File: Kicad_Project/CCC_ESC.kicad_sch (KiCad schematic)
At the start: 228 parts, among them J1 Conn_01x07, J2 Conn_01x06, J3 Conn_01x06, J4 Conn_01x06, SW1 Conn_01x02, U1 NCP5183 / TF2190-TAH, U2 NCP5183 / TF2190-TAH, U3 NCP5183 / TF2190-TAH, U4 NCS20034DR2G, U5 STM32F401CCU6_Balckpill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

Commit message: more layout
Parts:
- removed TpGS1: TestPoint, TestPoint:TestPoint_THTPad_D4.0mm_Drill2.0mm, symbol Connector:TestPoint
- removed TpGS3, TpGS5: TestPoint, TestPoint:TestPoint_THTPad_D1.5mm_Drill0.7mm, symbol Connector:TestPoint
- D1, D2, D3: footprint Diode_SMD:D_SMA -> Diode_SMD:D_SOD-123; LCSC C412437 -> C5290222
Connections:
- net AU_GATESIG renamed DV1H_P
- net BU_GATESIG renamed DV2H_P
- net CU_GATESIG renamed DV3H_P
- net PHASE_A renamed DV1H_N
- net PHASE_B renamed DV2H_N
- net PHASE_C renamed DV3H_N

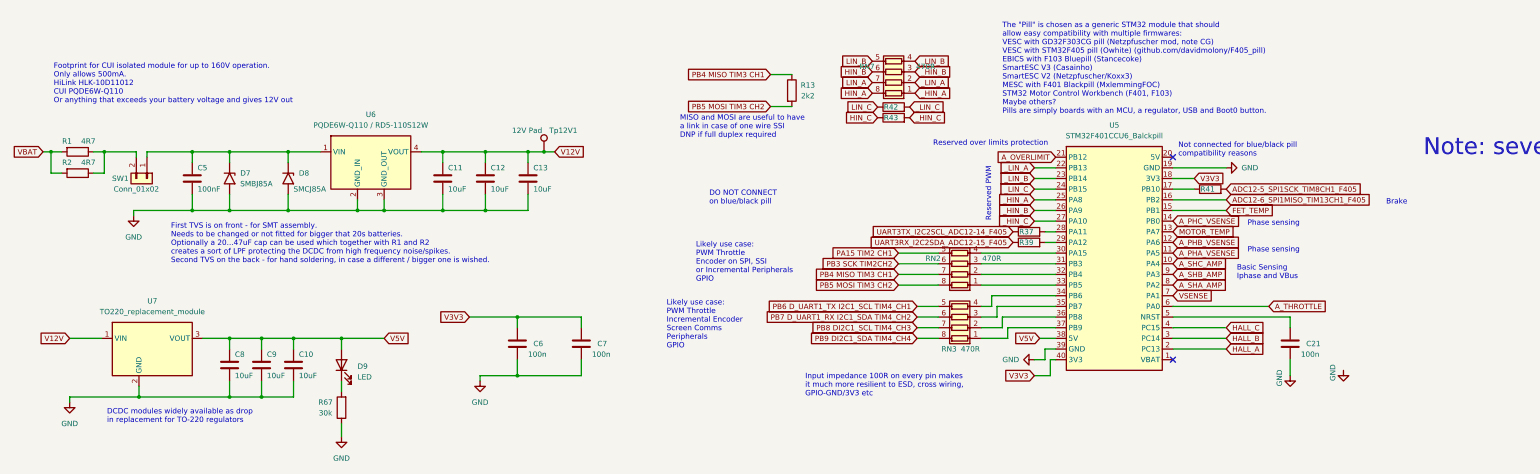
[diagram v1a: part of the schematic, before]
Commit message: added thermistor, 12v zener
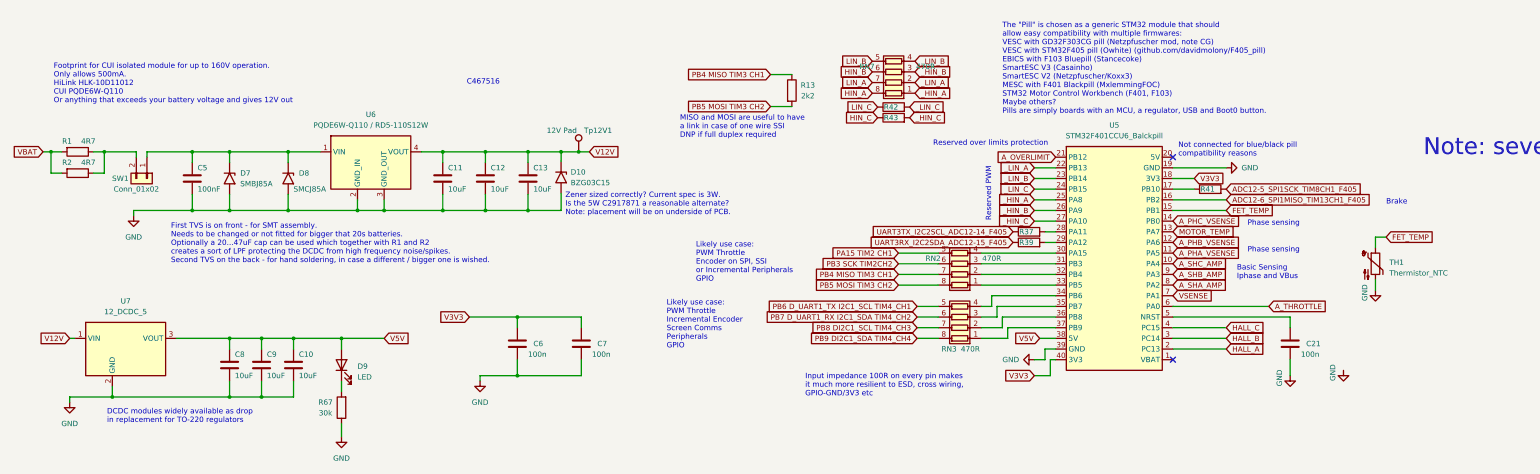
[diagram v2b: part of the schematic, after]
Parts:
- added D10: BZG03C15, Diode_SMD:D_SMA, symbol Diode:SM6T75A
- added TH1: Thermistor_NTC, Resistor_SMD:R_0603_1608Metric, symbol Device:Thermistor_NTC
- U7: value TO220_replacement_module -> 12_DCDC_5; footprint CCC_ESC_Custom_parts:TO220_replacement_module -> CCC_ESC_Custom_parts:12_DCDC_5
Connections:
- net FET_TEMP: now also TH1.1
- net GND: now also D10.2 (A2), TH1.2
- net V12V: now also D10.1 (A1)
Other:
- note added: "C467516"
- note added: "Zener sized correctly? Current spec is 3W. Is the 5W C2917871 a reasonable alternate? Note: placement will be on underside of PCB."
- note removed: "DO NOT CONNECT on blue/black pill"
- moved on the sheet: Tp12V1, U7

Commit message: added docs, prettied up fills
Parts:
- removed C31: 47pF, Capacitor_SMD:C_0603_1608Metric, symbol Device:C
- added C33: 10nF, Capacitor_SMD:C_0603_1608Metric, symbol Device:C
- C29, C30: value 47pF -> 10nF; LCSC C1671 -> C57112; MFR PT CL10C470JB8NNNC -> 0603B103K500NT
- CGS1, CGS10, CGS13, CGS16, CGS4, CGS7: value 6pF -> 6nF
- QB5: footprint Package_DFN_QFN:DFNW-8_L8.3-W8.4-P2.00-BL -> NVMTSC4D3N15MC:NVMTSC4D3N15MC
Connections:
- net A_PHA_VSENSE: now also C33.1; no longer C29.1
- net A_PHB_VSENSE: now also C29.1; no longer C30.1
- net A_PHC_VSENSE: now also C30.1
- net GND: now also C33.2
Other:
- note added: "Changes, not necessarily improvements: MOSFETS changed to DFNW format (NVMTSC4D3N15MC) Tidied up differential routing to shunt resistors and gate ressistors Added gate to source capacitors (CGS1-18) Protective 470 ohm resistors (RN7) between the drivers and PWM pill pins Phase sense caps (C29, C30, C33) set to 10nF for 10kHz range filtering Restructured vbat and gnd buses Restructured phase buses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"
- note added: "Use 10nF for a response in the 10kHz kind of range."
- note removed: "Note: several test points were removed in order to add additional components."
- moved on the sheet: C20, C22, C23, C24, C25, D4, D5, D6, R16, R17, R18, R19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

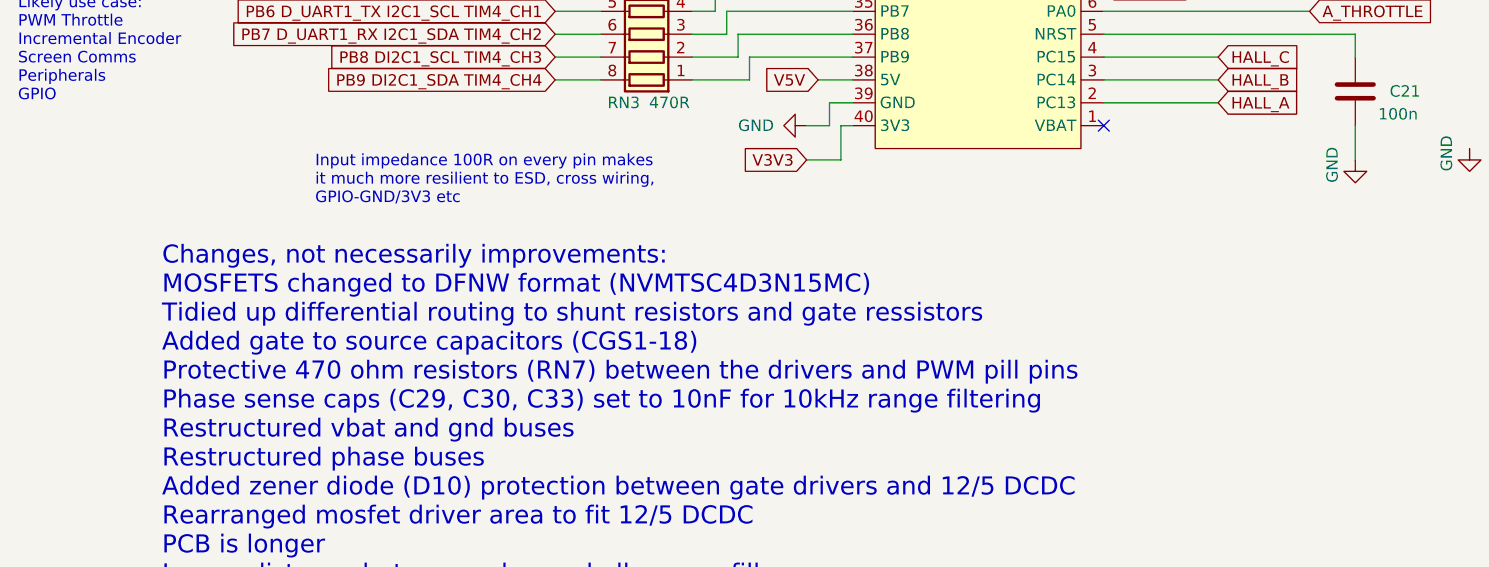
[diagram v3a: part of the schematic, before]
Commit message: new DFN footprints, changed some routes
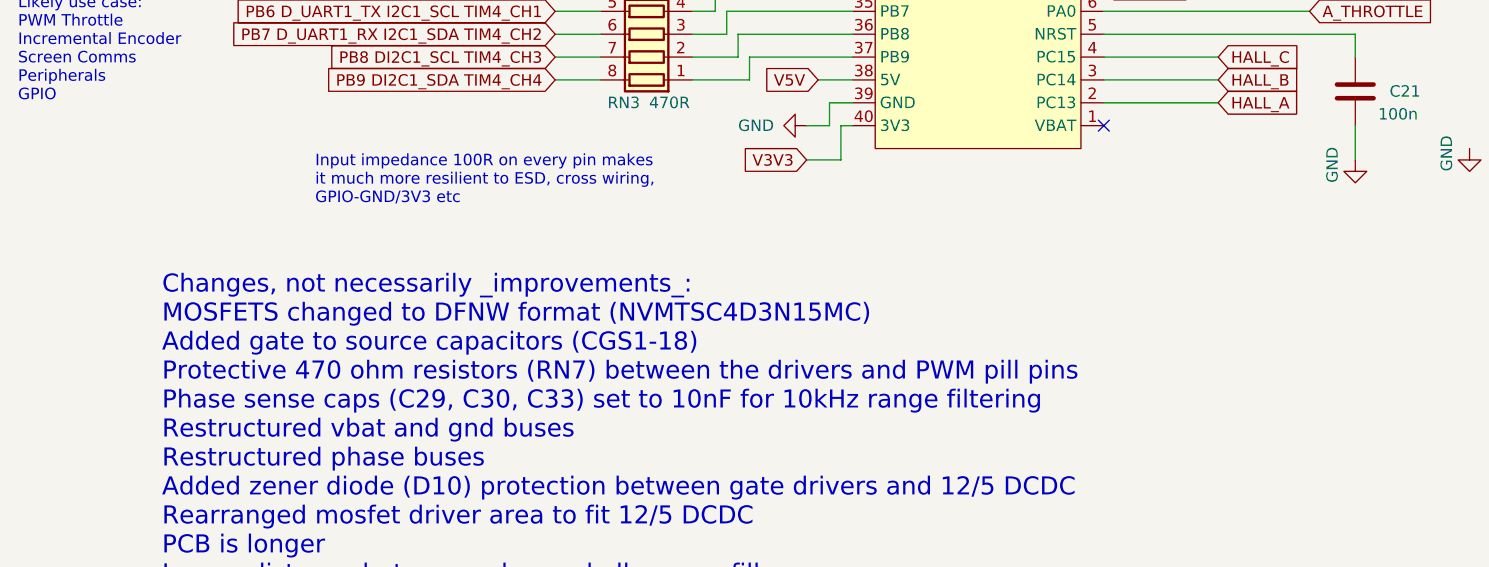
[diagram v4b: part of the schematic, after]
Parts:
- CGS11, CGS12, CGS14, CGS15, CGS17, CGS18, CGS2, CGS3, CGS5, CGS6, CGS8, CGS9: value 6pF -> 6nF
- QA1, QA2, QA3, QA4, QA5, QA6, QB1, QB2, QB3, QB4, QB6, QC1, QC2, QC3, QC4, QC5, QC6: footprint Package_DFN_QFN:DFNW-8_L8.3-W8.4-P2.00-BL -> NVMTSC4D3N15MC:custom_NVMTSC4D3N15MC; LCSC (none) -> C3280341
- QB5: footprint NVMTSC4D3N15MC:NVMTSC4D3N15MC -> NVMTSC4D3N15MC:custom_NVMTSC4D3N15MC; LCSC (none) -> C3280341
- R42, R43: LCSC (none) -> C23179
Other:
- note added: "Changes, not necessarily _improvements_: MOSFETS changed to DFNW format (NVMTSC4D3N15MC) Added gate to source capacitors (CGS1-18) Protective 470 ohm resistors (RN7) between the drivers and PWM pill pins Phase sense caps (C29, C30, C33) set to 10nF for 10kHz range filtering Restructured vbat and gnd buses Restructured phase buses Added zener diode (D10) protection between gate drivers and 12/5 DC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"
- note removed: "Changes, not necessarily improvements: MOSFETS changed to DFNW format (NVMTSC4D3N15MC) Tidied up differential routing to shunt resistors and gate ressistors Added gate to source capacitors (CGS1-18) Protective 470 ohm resistors (RN7) between the drivers and PWM pill pins Phase sense caps (C29, C30, C33) set to 10nF for 10kHz range filtering Restructured vbat and gnd buses Restructured phase buses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"

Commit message: minor touchups
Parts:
- CGS1, CGS10, CGS11, CGS12, CGS13, CGS14, CGS15, CGS16, CGS17, CGS18, CGS2, CGS3, CGS4, CGS5, CGS6, CGS7, CGS8, CGS9: value 6nF -> 4.7nF; LCSC (none) -> C597214
- QA1, QA2, QA3, QA4, QA5, QA6, QB1, QB2, QB3, QB4, QB5, QB6, QC1, QC2, QC3, QC4, QC5, QC6: MFR PT (none) -> NVMTSC4D3N15MC
- U4: LCSC C89848 -> C695777; MFR PT NCS20034DR2G -> COS724SR
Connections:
- net DVRL2: now reaches R50.2, RG10.1, RG11.2, RG12.2, TpGS4.1, U2.4 (DRVL)
- net AL_GATESIG renamed DVRL1
- net CL_GATESIG renamed DVRL3
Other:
- note added: "?????"
- note added: "Please confirm C531304 is correct specs"

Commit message: minor touchups
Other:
- note added: "MP2-DFN PUNCHLIST: Clean / uninterupted VBus and GND layers Restructured vbat and gnd buses for copper bus bars Restructured phase buses Differential lines for shunt resistors Heatsink mounting holes Different lines for (DRVH with HB) (DRV + GND) MOSFETS changed to DFNW format (NVMTSC4D3N15MC) Added gate to source 4.7nF capacitors (CGS1-18) Protective 470 ohm resistors (RN7) between the drivers a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"
- note removed: "Changes, not necessarily _improvements_: MOSFETS changed to DFNW format (NVMTSC4D3N15MC) Added gate to source capacitors (CGS1-18) Protective 470 ohm resistors (RN7) between the drivers and PWM pill pins Phase sense caps (C29, C30, C33) set to 10nF for 10kHz range filtering Restructured vbat and gnd buses Restructured phase buses Added zener diode (D10) protection between gate drivers and 12/5 DC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"
- moved on the sheet: C11, C12, C13, C21, C5, D10, D7, D8, R1, R13, R2, R37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

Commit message: second draft ready for review
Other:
- note added: "Caps for pill"
- note added: "Confirm zener sized correctly? Current spec is 3W. Is the 5W C2917871 a reasonable alternate? Note: placement will be on underside of PCB."
- note added: "This was 47pF. Use 10nF for a response in the 10kHz kind of range."
- note removed: "?????"
- note removed: "Use 10nF for a response in the 10kHz kind of range."
- note removed: "Zener sized correctly? Current spec is 3W. Is the 5W C2917871 a reasonable alternate? Note: placement will be on underside of PCB."
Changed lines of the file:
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@@
     (effects (font (size 1.27 1.27)) (justify left bottom))
   )
-  (text "MP2-DFN PUNCHLIST:\n	Clean / uninterupted VBus and GND layers\n	Restructured vbat and gnd buses for copper bus bars\n	Restructured phase buses\n	Differential lines for shunt resistors\n	Heatsink mounting holes\n	Different lines for (DRVH with HB) (DRV + GND)\n	MOSFETS changed to DFNW format (NVMTSC4D3N15MC)\n	Added gate to source 4.7nF capacitors (CGS1-18)\n	Protective 470 ohm resistors (RN7) between the drivers and PWM pill pins\n	Phase sense caps (C29, C30, C33) set to 10nF for 10kHz range filtering\n	Added zener diode (D10) protection between gate drivers and 12/5 DCDC\n	Rearranged mosfet driver area to fit 12/5 DCDC\n	Larger distance between edge and all copper fills\n	Added on board thermister\n	Restructured ceramic caps, added radial caps\n	Manual review of all parts / values / footprints in comparison to BOM\n	Removed many test points to conserve space. hopefully \n		pins can be soldered to FETs for testing."
+  (text "MP2-DFN PUNCHLIST:\n	Clean / uninterupted VBus and GND layers\n	Restructured vbat and gnd buses for copper bus bars\n	Restructured phase buses\n	Differential lines for shunt resistors\n	Heatsink mounting holes\n	Different lines for (DRVH with HB) (DRV + GND)\n	MOSFETS changed to DFNW format (NVMTSC4D3N15MC)\n	Added gate to source 4.7nF capacitors (CGS1-18)\n	Protective 470 ohm resistors (RN7) between the drivers and PWM pill pins\n	Phase sense caps (C29, C30, C33) set to 10nF for 10kHz range filtering\n	Added zener diode (D10) protection between gate drivers and 12/5 DCDC\n	Rearranged mosfet driver area to fit 12/5 DCDC\n	Larger distance between edge and all copper fills\n	Added on board thermister\n	Restructured ceramic caps, added radial caps\n	Manual review of all parts / values / footprints in comparison to BOM\n	Removed many test points to conserve space; pins can \n		be soldered to FETs for testing."
     (at 259.08 241.3 0)
     (effects (font (size 2 2)) (justify left bottom))
   )
-  (text "Use 10nF for a response in the 10kHz kind of range. "
-    (at 442.468 312.166 0)
+  (text "This was 47pF. Use 10nF for a response in \nthe 10kHz kind of range. "
+    (at 443.992 345.948 0)
     (effects (font (size 1.27 1.27)) (justify left bottom))
   )
@@
     (effects (font (size 1.27 1.27)) (justify left bottom))
   )
-  (text "?????" (at 338.582 316.23 0)
-    (effects (font (size 4 4)) (justify left bottom))
-  )
   (text "Fourth opamp used as overcurrent and voltage \ncomparator to protect against shoot through, \novercurrent + overvoltage in MCU crash\nIf any of the opamps outputs exceeds 3v3x8/2/(8.2+9.2) + diode forward voltage, \nthe opamp will pull low, which pulls PB12 low, triggering the STM32 hardware BRK\nTime constant approximately 0.47us\nThere's another 0.47us LPF on the F405 pill! That is not the case for Bluepill or Blackpill\n"
     (at 296.418 395.732 0)
@@
     (effects (font (size 1.27 1.27)) (justify left bottom))
   )
+  (text "Caps for pill" (at 132.588 168.656 0)
+    (effects (font (size 1.27 1.27)) (justify left bottom))
+  )
   (text "Reserved PWM\n" (at 260.35 133.35 90)
     (effects (font (size 1.27 1.27)) (justify left bottom))
   )
-  (text "Zener sized correctly? Current spec is 3W.\nIs the 5W C2917871 a reasonable alternate?\nNote: placement will be on underside of PCB."
+  (text "Confirm zener sized correctly? Current spec is 3W.\nIs the 5W C2917871 a reasonable alternate?\nNote: placement will be on underside of PCB."
     (at 149.86 134.62 0)
     (effects (font (size 1.27 1.27)) (justify left bottom))
@@
         )
       )
-    )
-  )
-  (symbol (lib_id "power:GND") (at 344.17 168.91 0) (unit 1)
-    (in_bom yes) (on_board yes) (dnp no)
-    (property "Reference" "#PWR02" (at 344.17 175.26 0)
-      (effects (font (size 1.27 1.27)) hide)
-    )
-    (property "Value" "GND" (at 341.63 171.45 90)
-      (effects (font (size 1.27 1.27)) (justify left))
-    )
-    (property "Footprint" "" (at 344.17 168.91 0)
-      (effects (font (size 1.27 1.27)) hide)
-    )
-    (property "Datasheet" "" (at 344.17 168.91 0)
-      (effects (font (size 1.27 1.27)) hide)
-    )
-    (pin "1")
-    (instances
-      (project "CCC_ESC"
-        (path "/31a3399e-b0e0-4a61-aacb-f319bb9df4d3"
-          (reference "#PWR02") (unit 1)
-        )
-      )

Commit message: fixed most of DMs suggestions
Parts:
- added D11: DSK320, Diode_SMD:D_SOD-123, symbol Diode:SM4007
- D1, D2, D3: value US1M -> DSK320; MFR PT US1M -> DSK320
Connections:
- net V12V: now also D11.1 (K); no longer C11.1, C12.1, C13.1, D10.1 (A1), Tp12V1.1, U6.4 (VOUT), U7.1 (VIN)
- new net V12V_safe: C11.1, C12.1, C13.1, D10.1 (A1), D11.2 (A), Tp12V1.1, U6.4 (VOUT), U7.1 (VIN)
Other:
- note added: "--> Onward to drivers, where dragons reside"
- note added: "--> Protect logic board"
- note removed: "DCDC modules widely available as drop in replacement for TO-220 regulators"
- moved on the sheet: C10, C6, C7, C8, C9, D10, D9, R67, Tp12V1, U7
